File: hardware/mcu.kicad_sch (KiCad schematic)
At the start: 26 parts, among them J6 Debug, SW1 BOOT, SW2 RESET, U2 STM32F405RGTx, Y1 8MHz

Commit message: Layout mostly done
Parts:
- removed H5: Heatsink, MountingHole:MountingHole_3.2mm_M3_Pad, symbol Mechanical:MountingHole_Pad
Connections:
- net HALL1: now also U2.39 (PC8); no longer U2.37 (PC6)
- net HALL3: now also U2.37 (PC6); no longer U2.39 (PC8)
- net T1: no longer names the net of U2.17 (PA3)
- net T2: no longer names the net of U2.26 (PB0)
- net T3: no longer names the net of U2.27 (PB1)
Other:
- moved on the sheet: H3, H4
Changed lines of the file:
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@@
 		)
 	)
-	(hierarchical_label "T2"
-		(shape input)
-		(at 187.96 105.41 0)
-		(effects
-			(font
-				(size 1.27 1.27)
-			)
-			(justify left)
-		)
-	)
 	(hierarchical_label "V1"
 		(shape input)
@@
 		)
 	)
-	(hierarchical_label "T1"
-		(shape input)
-		(at 187.96 69.85 0)
-		(effects
-			(font
-				(size 1.27 1.27)
-			)
-			(justify left)
-		)
-	)
 	(hierarchical_label "L3"
 		(shape output)
@@
 		)
 	)
-	(hierarchical_label "T3"
-		(shape input)
-		(at 187.96 107.95 0)
-		(effects
-			(font
-				(size 1.27 1.27)
-			)
-			(justify left)
-		)
-	)
 	(hierarchical_label "LED_RED"
 		(shape output)
@@
 	(hierarchical_label "HALL3"
 		(shape input)
-		(at 147.32 105.41 180)
+		(at 147.32 100.33 180)
 		(effects
 			(font
@@
 	(hierarchical_label "HALL1"
 		(shape input)
-		(at 147.32 100.33 180)
+		(at 147.32 105.41 180)
 		(effects
 			(font
@@
 	)
 	(symbol
-		(lib_id "Mechanical:MountingHole_Pad")
-		(at 251.46 138.43 0)
-		(unit 1)
-		(exclude_from_sim no)
-		(in_bom no)
-		(on_board yes)
-		(dnp no)
-		(fields_autoplaced yes)
-		(property "Reference" "H5"
-			(at 254 135.8899 0)
-			(effects
-				(font
-					(size 1.27 1.27)
-				)
-				(justify left)
-			)
-		)
-		(property "Value" "Heatsink"
-			(at 254 138.4299 0)
-			(effects
-				(font
-					(size 1.27 1.27)
-				)
-				(justify left)
-			)
-		)
-		(property "Footprint" "MountingHole:MountingHole_3.2mm_M3_Pad"
-			(at 251.46 138.43 0)
-			(effects
-				(font
-					(size 1.27 1.27)
-				)
-				(hide yes)
-			)
-		)
-		(property "Datasheet" "~"
-			(at 251.46 138.43 0)
-			(effects
-				(font
-					(size 1.27 1.27)
-				)
-				(hide yes)
-			)
-		)
-		(property "Description" "Mounting Hole with connection"
-			(at 251.46 138.43 0)
-			(effects
-				(font
-					(size 1.27 1.27)
-				)
-				(hide yes)
-			)
-		)
-		(pin "1"
-		)
-		(instances
-			(project "greenmobi-drive"
-				(path "/a12b77e7-bd0f-4a70-9ba2-19a87ce48819/7c031b43-26d1-47e4-bdd2-d28a8add82c7"
-					(reference "H5")
-					(unit 1)
-				)
-			)
-		)
-	)
-	(symbol
 		(lib_id "Switch:SW_Push")
 		(at 74.93 49.53 90)
@@
 	(symbol
 		(lib_id "Mechanical:MountingHole_Pad")
-		(at 243.84 149.86 0)
+		(at 243.84 138.43 0)
 		(unit 1)
 		(exclude_from_sim no)
@@
 		(fields_autoplaced yes)
 		(property "Reference" "H3"
-			(at 246.38 147.3199 0)
+			(at 246.38 135.8899 0)
 			(effects
 				(font
@@
 		)
 		(property "Value" "Heatsink"
-			(at 246.38 149.8599 0)
+			(at 246.38 138.4299 0)
 			(effects
 				(font
@@
 		)
 		(property "Footprint" "MountingHole:MountingHole_3.2mm_M3_Pad"
-			(at 243.84 149.86 0)
+			(at 243.84 138.43 0)
 			(effects
 				(font
@@
 		)
 		(property "Datasheet" "~"
-			(at 243.84 149.86 0)
+			(at 243.84 138.43 0)
 			(effects
 				(font
@@
 		)
 		(property "Description" "Mounting Hole with connection"
-			(at 243.84 149.86 0)
+			(at 243.84 138.43 0)
 			(effects
 				(font
@@
 	(symbol
 		(lib_id "power:GND")
-		(at 251.46 140.97 0)
-		(unit 1)
-		(exclude_from_sim no)
-		(in_bom yes)
-		(on_board yes)
-		(dnp no)
-		(fields_autoplaced yes)
-		(property "Reference" "#PWR089"
-			(at 251.46 147.32 0)
-			(effects
-				(font
-					(size 1.27 1.27)
-				)
-				(hide yes)
-			)
-		)
-		(property "Value" "GND"
-			(at 251.46 146.05 0)
-			(effects
-				(font
-					(size 1.27 1.27)
-				)
-			)
-		)
-		(property "Footprint" ""
-			(at 251.46 140.97 0)
-			(effects
-				(font
-					(size 1.27 1.27)
-				)
-				(hide yes)
-			)
-		)
-		(property "Datasheet" ""
-			(at 251.46 140.97 0)
-			(effects
-				(font
-					(size 1.27 1.27)
-				)
-				(hide yes)
-			)
-		)
-		(property "Description" "Power symbol creates a global label with name \"GND\" , ground"
-			(at 251.46 140.97 0)
-			(effects
-				(font
-					(size 1.27 1.27)
-				)
-				(hide yes)
-			)
-		)
-		(pin "1"
-		)
-		(instances
-			(project "greenmobi-drive"
-				(path "/a12b77e7-bd0f-4a70-9ba2-19a87ce48819/7c031b43-26d1-47e4-bdd2-d28a8add82c7"
-					(reference "#PWR089")
-					(unit 1)
-				)
-			)
-		)
-	)
-	(symbol
-		(lib_id "power:GND")
 		(at 119.38 88.9 0)
 		(unit 1)
@@
 	(symbol
 		(lib_id "power:GND")
-		(at 243.84 152.4 0)
+		(at 243.84 140.97 0)
 		(unit 1)
 		(exclude_from_sim no)
@@
 		(fields_autoplaced yes)
 		(property "Reference" "#PWR087"
-			(at 243.84 158.75 0)
+			(at 243.84 147.32 0)
 			(effects
 				(font
@@
 		)
 		(property "Value" "GND"
-			(at 243.84 157.48 0)
+			(at 243.84 146.05 0)
 			(effects
 				(font
@@
 		)
 		(property "Footprint" ""
-			(at 243.84 152.4 0)
+			(at 243.84 140.97 0)
 			(effects
 				(font
@@
 		)
 		(property "Datasheet" ""
-			(at 243.84 152.4 0)
+			(at 243.84 140.97 0)
 			(effects
 				(font
@@
 		)
 		(property "Description" "Power symbol creates a global label with name \"GND\" , ground"
-			(at 243.84 152.4 0)
+			(at 243.84 140.97 0)
 			(effects
 				(font
@@
 		)
 		(pin "46"
-			(alternate "SYS_JTMS-SWDIO")
 		)
 		(pin "18"
@@
 		)
 		(pin "55"
-			(alternate "SYS_JTDO-SWO")
 		)
 		(pin "28"
 		)
 		(pin "62"
-			(alternate "CAN1_TX")
 		)
 		(pin "27"
-			(alternate "ADC1_IN9")
 		)
 		(pin "64"
@@
 		)
 		(pin "61"
-			(alternate "CAN1_RX")
 		)
 		(pin "29"
 		)
 		(pin "16"
-			(alternate "ADC1_IN2")
 		)
 		(pin "45"
-			(alternate "USB_OTG_FS_DP")
 		)
 		(pin "53"
@@
 		)
 		(pin "17"
-			(alternate "ADC1_IN3")
 		)
 		(pin "3"
@@
 		)
 		(pin "15"
-			(alternate "ADC1_IN1")
 		)
 		(pin "5"
@@
 		)
 		(pin "14"
-			(alternate "ADC1_IN0")
 		)
 		(pin "43"
@@
 		)
 		(pin "44"
-			(alternate "USB_OTG_FS_DM")
 		)
 		(pin "32"
 		)
 		(pin "50"
-			(alternate "SYS_JTDI")
 		)
 		(pin "35"
@@
 		)
 		(pin "26"
-			(alternate "ADC1_IN8")
 		)
 		(pin "51"
@@
 		)
 		(pin "49"
-			(alternate "SYS_JTCK-SWCLK")
 		)
 		(pin "24"
@@
 	(symbol
 		(lib_id "Mechanical:MountingHole_Pad")
-		(at 257.81 149.86 0)
+		(at 257.81 138.43 0)
 		(unit 1)
 		(exclude_from_sim no)
@@
 		(fields_autoplaced yes)
 		(property "Reference" "H4"
-			(at 260.35 147.3199 0)
+			(at 260.35 135.8899 0)
 			(effects
 				(font
@@
 		)
 		(property "Value" "Heatsink"
-			(at 260.35 149.8599 0)
+			(at 260.35 138.4299 0)
 			(effects
 				(font
@@
 		)
 		(property "Footprint" "MountingHole:MountingHole_3.2mm_M3_Pad"
-			(at 257.81 149.86 0)
+			(at 257.81 138.43 0)
 			(effects
 				(font
@@
 		)
 		(property "Datasheet" "~"
-			(at 257.81 149.86 0)
+			(at 257.81 138.43 0)
 			(effects
 				(font
@@
 		)
 		(property "Description" "Mounting Hole with connection"
-			(at 257.81 149.86 0)
+			(at 257.81 138.43 0)
 			(effects
 				(font
@@
 	(symbol
 		(lib_id "power:GND")
-		(at 257.81 152.4 0)
+		(at 257.81 140.97 0)
 		(unit 1)
 		(exclude_from_sim no)
@@
 		(fields_autoplaced yes)
 		(property "Reference" "#PWR088"
-			(at 257.81 158.75 0)
+			(at 257.81 147.32 0)
 			(effects
 				(font
@@
 		)
 		(property "Value" "GND"
-			(at 257.81 157.48 0)
+			(at 257.81 146.05 0)
 			(effects
 				(font
@@
 		)
 		(property "Footprint" ""
-			(at 257.81 152.4 0)
+			(at 257.81 140.97 0)
 			(effects
 				(font
@@
 		)
 		(property "Datasheet" ""
-			(at 257.81 152.4 0)
+			(at 257.81 140.97 0)
 			(effects
 				(font
@@
 		)
 		(property "Description" "Power symbol creates a global label with name \"GND\" , ground"
-			(at 257.81 152.4 0)
+			(at 257.81 140.97 0)
 			(effects
 				(font

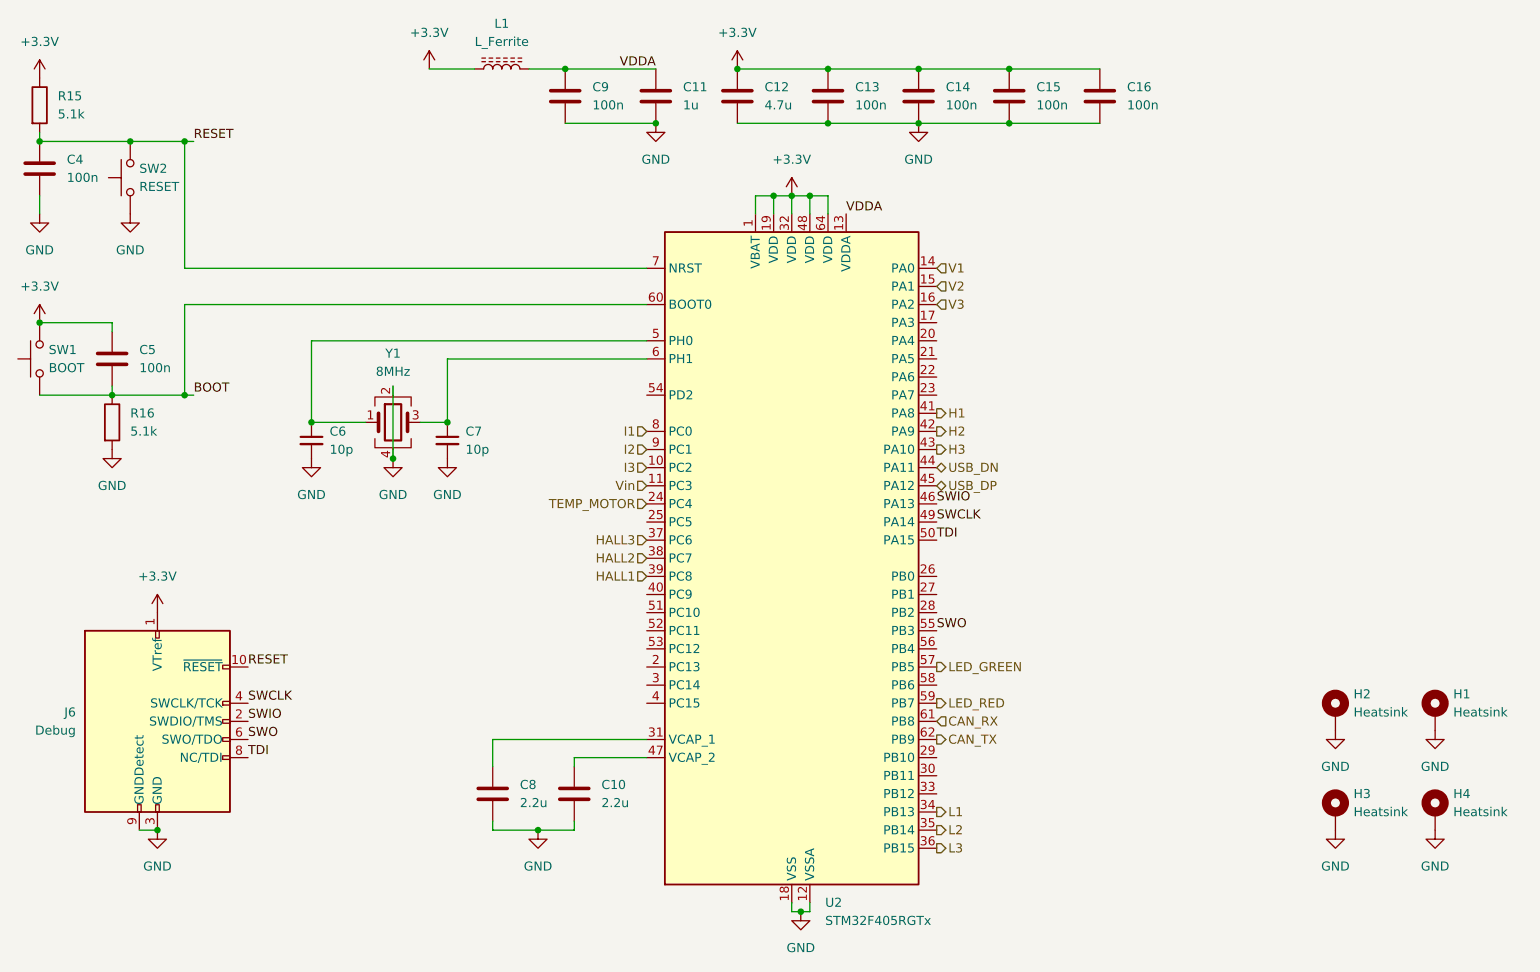
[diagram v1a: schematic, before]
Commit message: BOM optimizations
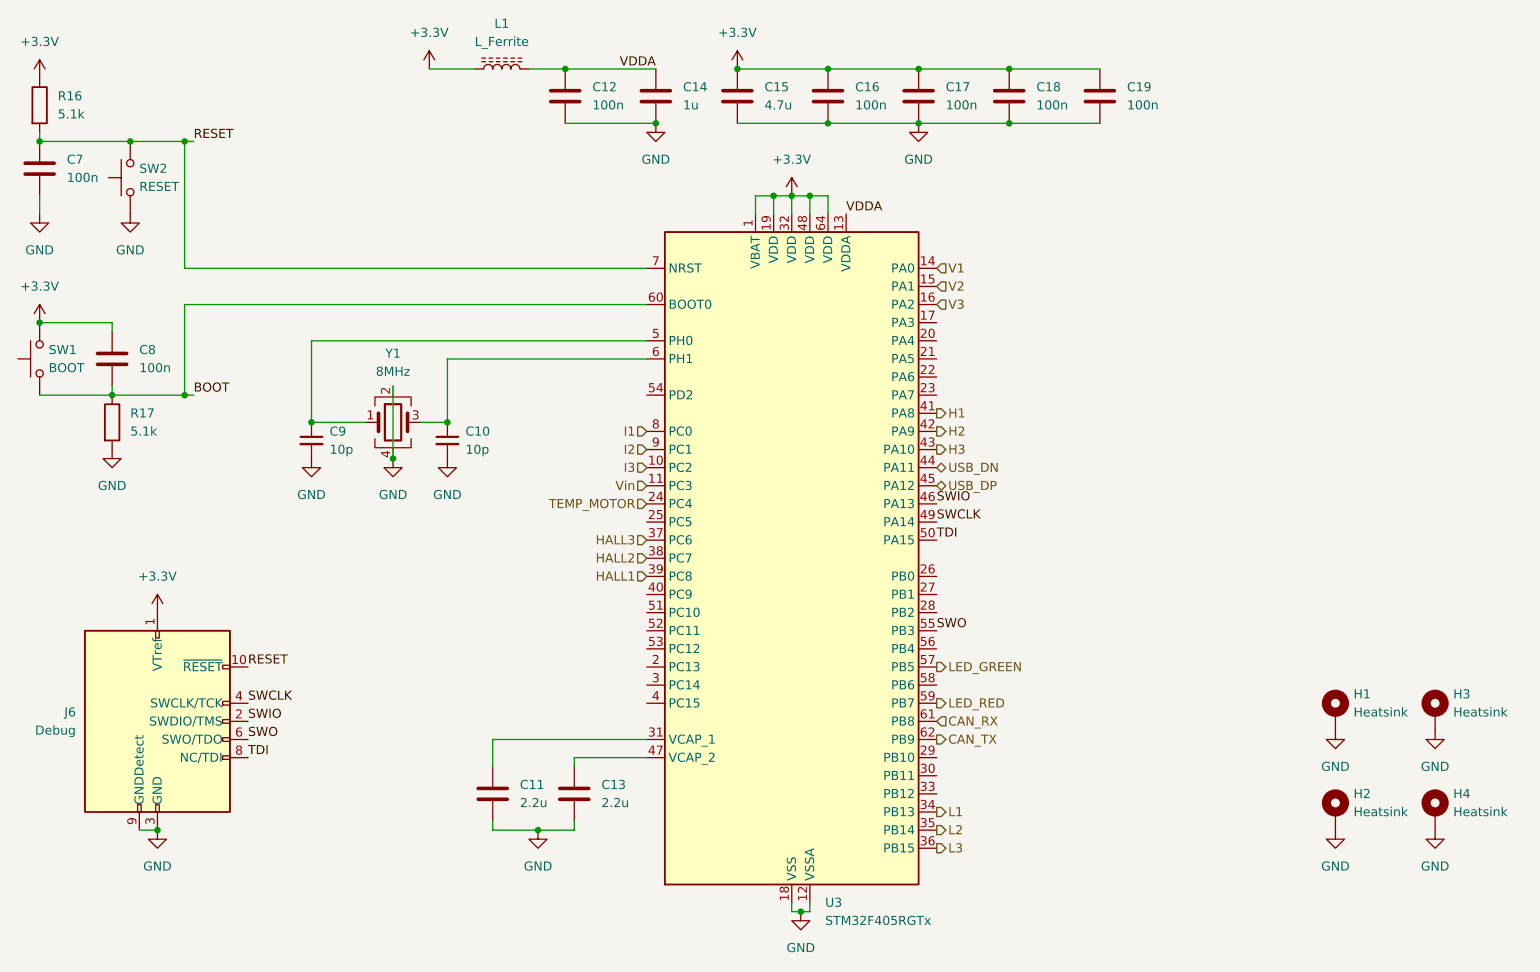
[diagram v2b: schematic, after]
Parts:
- renumbered C7 to C10, C8 to C11, C9 to C12, C10 to C13, C11 to C14, C12 to C15, C13 to C16, C14 to C17, C15 to C18, C16 to C19, C4 to C7, C5 to C8, C6 to C9, H2 to H1, H3 to H2, H1 to H3, R15 to R16, R16 to R17, U2 to U3

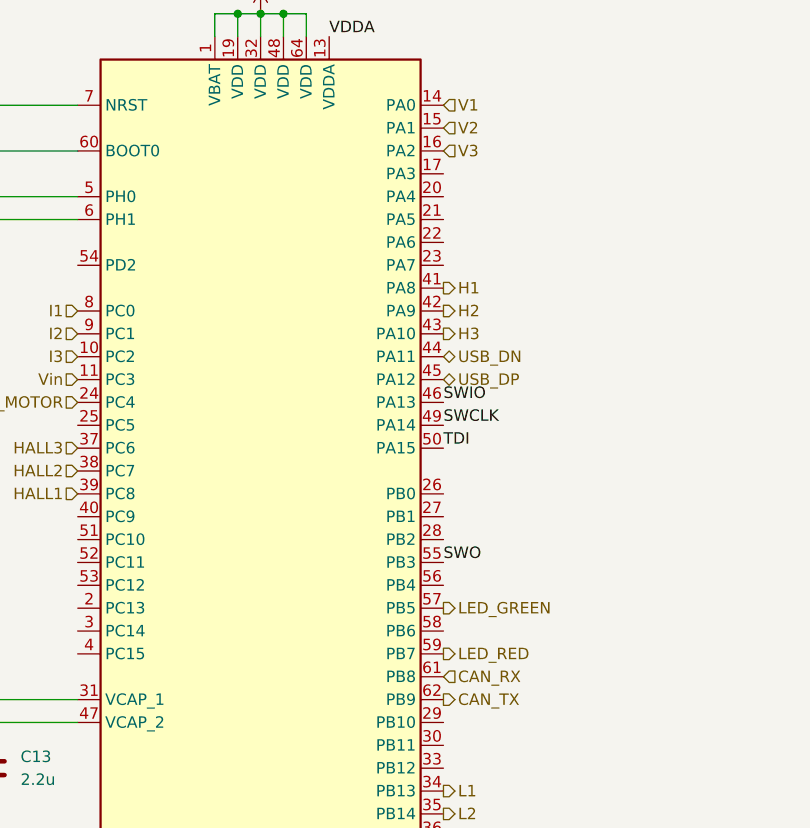
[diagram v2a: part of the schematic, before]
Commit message: Mounting holes alignment
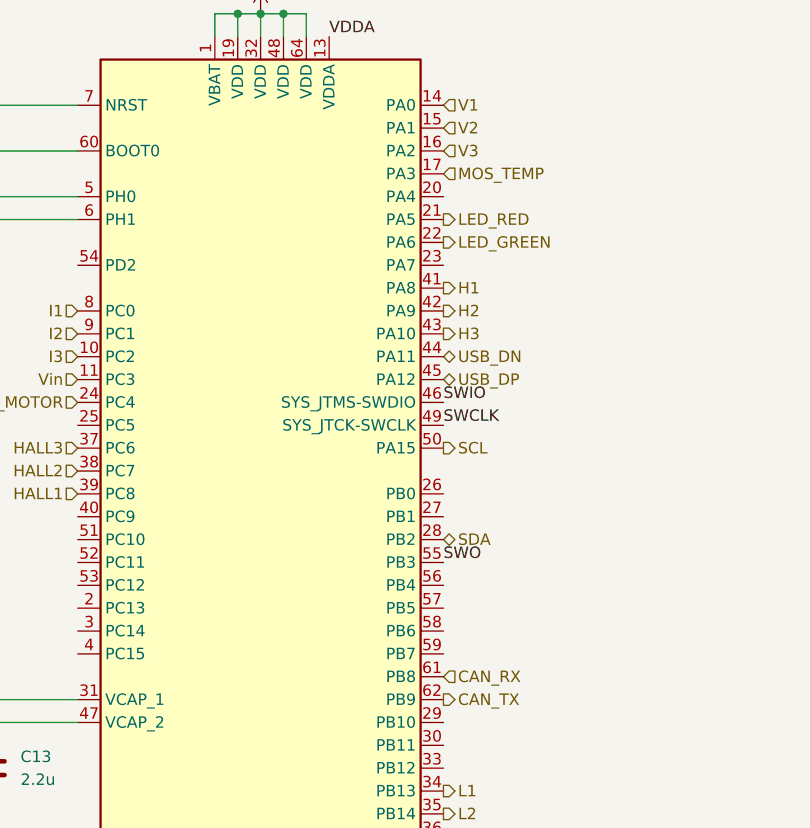
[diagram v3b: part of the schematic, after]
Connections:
- net LED_GREEN: now also U3.22 (PA6); no longer U3.57 (PB5)
- net LED_RED: now also U3.21 (PA5); no longer U3.59 (PB7)
- net TDI: no longer U3.50 (PA15)
- net MOS_TEMP: now reaches U3.17 (PA3)
- net SDA: now reaches U3.28 (PB2)
- new net SCL: U3.50 (PA15)
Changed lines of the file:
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@@
 		)
 	)
-	(label "TDI"
-		(at 187.96 100.33 0)
-		(effects
-			(font
-				(size 1.27 1.27)
-			)
-			(justify left bottom)
-		)
-	)
 	(label "SWO"
 		(at 91.44 128.27 0)
@@
 		)
 	)
+	(hierarchical_label "SCL"
+		(shape output)
+		(at 187.96 100.33 0)
+		(effects
+			(font
+				(size 1.27 1.27)
+			)
+			(justify left)
+		)
+	)
 	(hierarchical_label "I1"
 		(shape input)
@@
 		)
 	)
+	(hierarchical_label "MOS_TEMP"
+		(shape input)
+		(at 187.96 69.85 0)
+		(effects
+			(font
+				(size 1.27 1.27)
+			)
+			(justify left)
+		)
+	)
 	(hierarchical_label "LED_RED"
 		(shape output)
-		(at 187.96 123.19 0)
+		(at 187.96 74.93 0)
 		(effects
 			(font
@@
 		)
 	)
+	(hierarchical_label "SDA"
+		(shape bidirectional)
+		(at 187.96 110.49 0)
+		(effects
+			(font
+				(size 1.27 1.27)
+			)
+			(justify left)
+		)
+	)
 	(hierarchical_label "LED_GREEN"
 		(shape output)
-		(at 187.96 118.11 0)
+		(at 187.96 77.47 0)
 		(effects
 			(font
@@
 		)
 		(pin "46"
+			(alternate "SYS_JTMS-SWDIO")
 		)
 		(pin "18"
@@
 		)
 		(pin "49"
+			(alternate "SYS_JTCK-SWCLK")
 		)
 		(pin "24"

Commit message: Capacitors sourced
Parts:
- C10, C9: LCSC (none) -> C526994
- C11, C13: LCSC (none) -> C170151
- C12, C16, C17, C18, C19, C7, C8: LCSC (none) -> C77020
- C14: LCSC (none) -> C14445
- C15: LCSC (none) -> C23733
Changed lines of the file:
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@@
 			)
 		)
-		(property "Sim.Type" ""
-			(at 127 34.29 90)
-			(effects
-				(font
-					(size 1.27 1.27)
-				)
-				(hide yes)
-			)
-		)
 		(pin "2"
 		)
@@
 			)
 		)
-		(property "Sim.Type" ""
-			(at 78.74 125.73 0)
-			(effects
-				(font
-					(size 1.27 1.27)
-				)
-				(hide yes)
-			)
-		)
 		(pin "6"
 		)
@@
 			)
 		)
-		(property "Sim.Type" ""
-			(at 74.93 49.53 90)
-			(effects
-				(font
-					(size 1.27 1.27)
-				)
-				(hide yes)
-			)
-		)
 		(pin "2"
 		)
@@
 			)
 		)
-		(property "Sim.Type" ""
+		(property "LCSC" "C77020"
 			(at 72.39 74.93 0)
 			(effects
@@
 			)
 		)
-		(property "Sim.Type" ""
-			(at 62.23 74.93 90)
-			(effects
-				(font
-					(size 1.27 1.27)
-				)
-				(hide yes)
-			)
-		)
 		(pin "2"
 		)
@@
 			)
 		)
-		(property "Sim.Type" ""
+		(property "LCSC" "C77020"
 			(at 198.12 38.1 0)
 			(effects
@@
 			)
 		)
-		(property "Sim.Type" ""
+		(property "LCSC" "C77020"
 			(at 185.42 38.1 0)
 			(effects
@@
 			)
 		)
-		(property "Sim.Type" ""
-			(at 111.76 83.82 0)
-			(effects
-				(font
-					(size 1.27 1.27)
-				)
-				(hide yes)
-			)
-		)
 		(pin "4"
 		)
@@
 			)
 		)
-		(property "Sim.Type" ""
+		(property "LCSC" "C77020"
 			(at 172.72 38.1 0)
 			(effects
@@
 			)
 		)
-		(property "Sim.Type" ""
+		(property "LCSC" "C14445"
 			(at 148.59 38.1 0)
 			(effects
@@
 			)
 		)
-		(property "Sim.Type" ""
+		(property "LCSC" "C77020"
 			(at 135.89 38.1 0)
 			(effects
@@
 			)
 		)
-		(property "Sim.Type" ""
+		(property "LCSC" "C526994"
 			(at 100.33 86.36 0)
 			(effects
@@
 			)
 		)
-		(property "Sim.Type" ""
+		(property "LCSC" "C23733"
 			(at 160.02 38.1 0)
 			(effects
@@
 			)
 		)
-		(property "Sim.Type" ""
+		(property "LCSC" "C526994"
 			(at 119.38 86.36 0)
 			(effects
@@
 			)
 		)
-		(property "Sim.Type" ""
+		(property "LCSC" "C77020"
 			(at 62.23 48.26 0)
 			(effects
@@
 			)
 		)
-		(property "Sim.Type" ""
+		(property "LCSC" "C170151"
 			(at 137.16 135.89 0)
 			(effects
@@
 			)
 		)
-		(property "Sim.Type" ""
-			(at 72.39 83.82 0)
-			(effects
-				(font
-					(size 1.27 1.27)
-				)
-				(hide yes)
-			)
-		)
 		(pin "2"
 		)
@@
 			)
 		)
-		(property "Sim.Type" ""
+		(property "LCSC" "C77020"
 			(at 210.82 38.1 0)
 			(effects
@@
 			)
 		)
-		(property "Sim.Type" ""
+		(property "LCSC" "C170151"
 			(at 125.73 135.89 0)
 			(effects
@@
 			)
 		)
-		(property "Sim.Type" ""
-			(at 167.64 102.87 0)
-			(effects
-				(font
-					(size 1.27 1.27)
-				)
-				(hide yes)
-			)
-		)
 		(pin "58"
 		)
@@
 			(at 62.23 39.37 0)
 			(effects
-				(font
-					(size 1.27 1.27)
-				)
-				(hide yes)
-			)
-		)
-		(property "Sim.Type" ""
-			(at 62.23 39.37 0)
-			(effects

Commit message: Sourcing complete
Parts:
- J6: LCSC (none) -> C150517
- L1: value L_Ferrite -> 1k@100MHz; LCSC (none) -> C76883
- R16, R17: LCSC (none) -> C25905
- Y1: LCSC (none) -> C400090
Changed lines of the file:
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@@
 			)
 		)
-		(property "Value" "L_Ferrite"
+		(property "Value" "1k@100MHz"
 			(at 127 30.48 90)
 			(effects
@@
 			)
 		)
+		(property "LCSC" "C76883"
+			(at 127 34.29 90)
+			(effects
+				(font
+					(size 1.27 1.27)
+				)
+				(hide yes)
+			)
+		)
 		(pin "2"
 		)
@@
 			)
 		)
+		(property "LCSC" "C150517"
+			(at 78.74 125.73 0)
+			(effects
+				(font
+					(size 1.27 1.27)
+				)
+				(hide yes)
+			)
+		)
 		(pin "6"
 		)
@@
 			)
 		)
+		(property "LCSC" "C400090"
+			(at 111.76 83.82 0)
+			(effects
+				(font
+					(size 1.27 1.27)
+				)
+				(hide yes)
+			)
+		)
 		(pin "4"
 		)
@@
 			)
 		)
+		(property "LCSC" "C25905"
+			(at 72.39 83.82 0)
+			(effects
+				(font
+					(size 1.27 1.27)
+				)
+				(hide yes)
+			)
+		)
 		(pin "2"
 		)
@@
 			(at 62.23 39.37 0)
 			(effects
+				(font
+					(size 1.27 1.27)
+				)
+				(hide yes)
+			)
+		)
+		(property "LCSC" "C25905"
+			(at 62.23 39.37 0)
+			(effects
